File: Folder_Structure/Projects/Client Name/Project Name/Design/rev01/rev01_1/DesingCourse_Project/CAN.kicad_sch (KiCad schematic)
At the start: 0 parts

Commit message: Update 6
SCH and LIB for MOSFET page done, missing passive components
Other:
- company: (none) -> Integro Consulting AB
- title: (none) -> PCB Mastery Project
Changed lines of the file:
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@@
 	(generator_version "9.0")
 	(paper "A4")
+	(title_block
+		(title "PCB Mastery Project")
+		(date "2026-01-27")
+		(rev "001")
+		(company "Integro Consulting AB")
+		(comment 1 "TBD")
+		(comment 2 "TBD")
+		(comment 3 "TBD")
+		(comment 4 "Josue Godinez")
+	)
 )

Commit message: Update 11
SCH finishe, missing the labels and logos and adding all passive components
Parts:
- added C50: 2u2, symbol Device:C
- added C51, C52: 51p, symbol Device:C
- added D15: ESDCAN24-2BLY, ESDCAN24-2BLY:SOT95P237X112-3N, symbol JGB_Library:ESDCAN24-2BLY
- added J1: 874380443, 874380843:MOLEX_874380443, symbol Molex_87438:874380443
- added L1: 744227S, WE-SL2:WE-SL2, symbol WE-SL2:744227S
- added R48, R51: 10R, symbol Device:R
- added R49: 10k, symbol Device:R
- added R50: 120R, symbol Device:R
- added U5: SN65HVD230D, SN65HVD230D:SOIC127P599X175-8N, symbol SN65HVD230D:SN65HVD230D
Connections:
- new net: R49.1, U5.8 (RS)
- new net CAN_N: L1.3, U5.6 (CANL)
- new net CAN_P: L1.4, U5.7 (CANH)
- new net CAN_RX: U5.4 (R)
- new net CAN_TX: U5.1 (D)
- new net CONN_CAN_N: C52.1, D15.2 (A2), J1.3_1 (3), J1.3_2 (3), R50.2, R51.1
- new net CONN_CAN_P: C51.1, D15.1 (A1), J1.2_1 (2), J1.2_2 (2), R48.1, R50.1
- new net GND: C50.2, C51.2, C52.2, D15.3 (C), J1.4_1 (4), J1.4_2 (4), R49.2, U5.2 (GND)
- new net P3V3: C50.1, U5.3 (VCC)
- new net P5V: J1.1_1 (1), J1.1_2 (1)
- new net R_CAN_N: L1.2, R51.2
- new net R_CAN_P: L1.1, R48.2
- no-connect marks 0 -> 1
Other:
- note added: "CAN"
- note added: "CAN_H & CAN_L"
- note added: "Mode selection resistor Slew rate of ~15V/us"
- note added: "Place as close as possible to the IC"
- note added: "ROUTE AS DIFF PAIR"

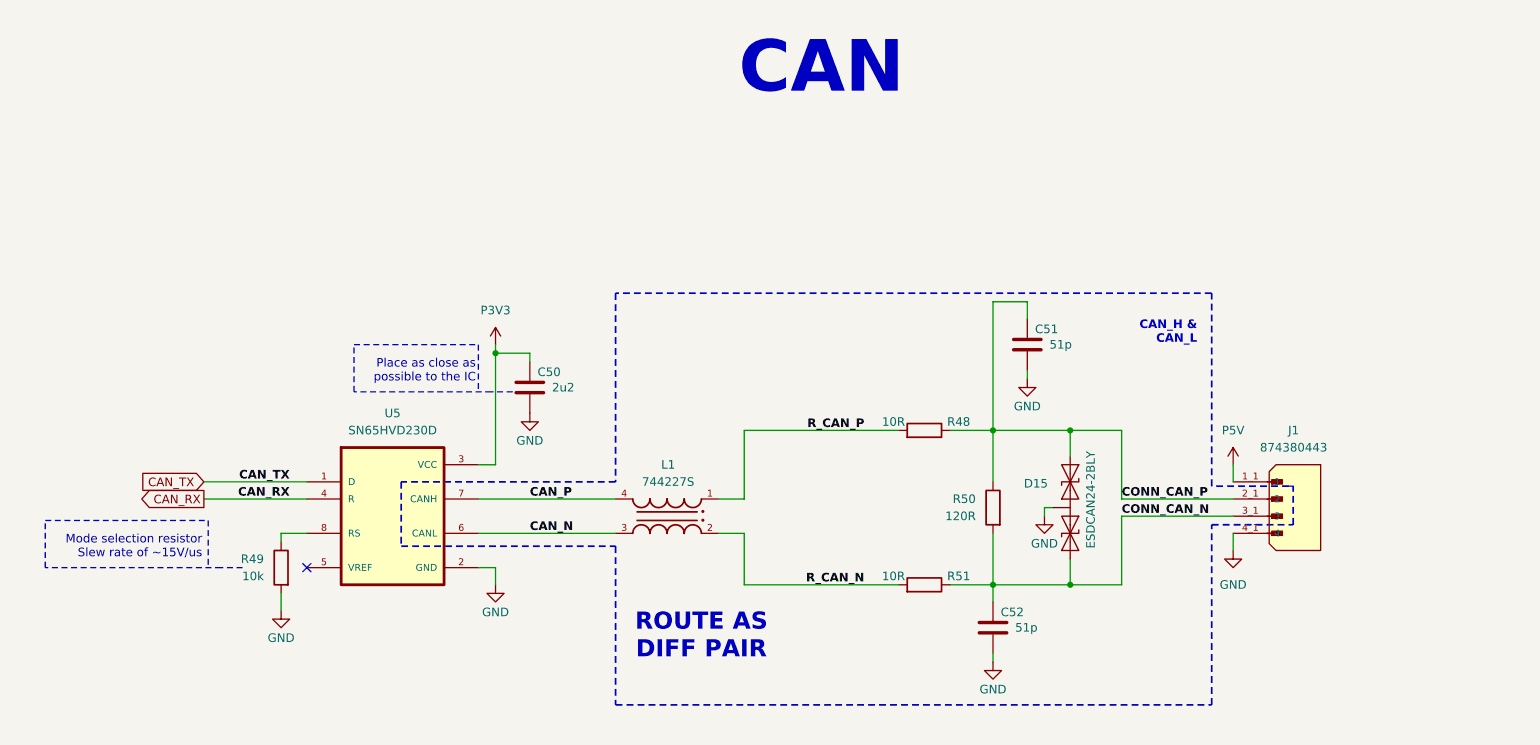
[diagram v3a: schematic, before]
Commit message: Update 12
Until STEP-DOWN page, all components have complete libraries.

Creation and incluison of all logos and labels libraries
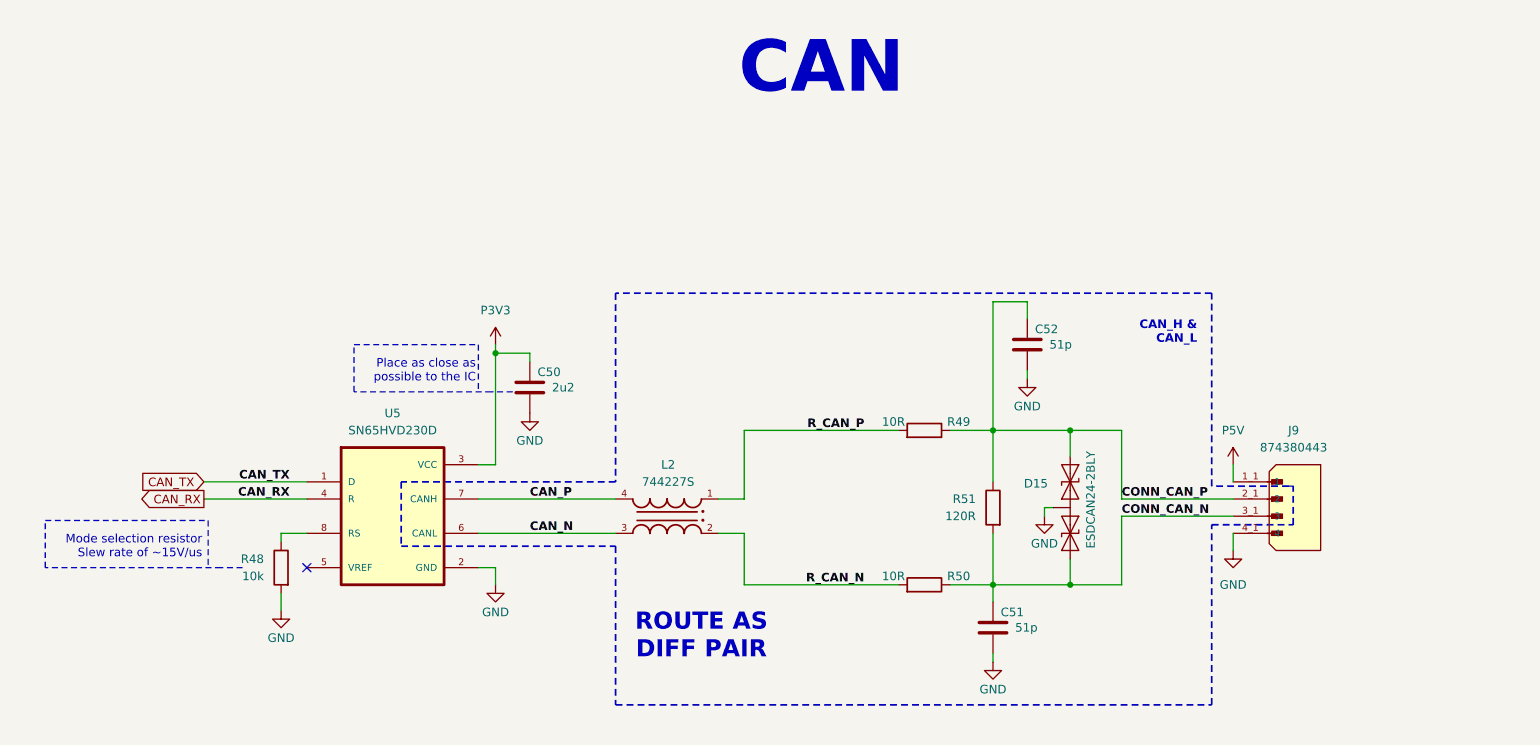
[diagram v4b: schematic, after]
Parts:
- renumbered C52 to C51, C51 to C52, J1 to J9, L1 to L2, R49 to R48, R48 to R49, R51 to R50, R50 to R51

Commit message: Update14
All components with FP, missing the block diagram
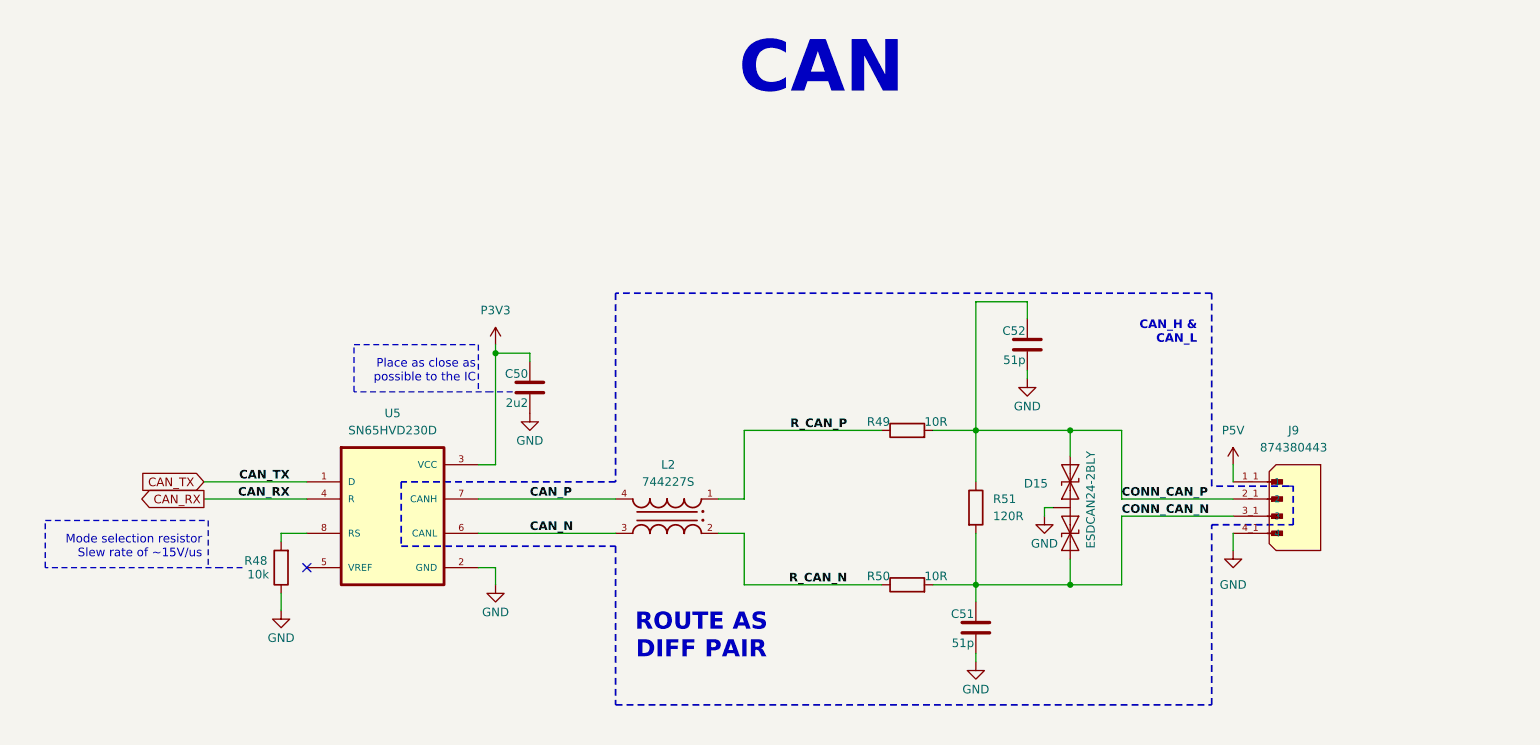
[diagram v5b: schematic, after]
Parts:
- C50: footprint (none) -> Capacitor_SMD:C_0603_1608Metric; Package (none) -> 0603; Temp Coeff (none) -> X5R; Tolerance (none) -> 10%; Voltage Rating (none) -> 6.3V
- C51, C52: footprint (none) -> Capacitor_SMD:C_0603_1608Metric; Package (none) -> 0603; Temp Coeff (none) -> NP0; Tolerance (none) -> 10%; Voltage Rating (none) -> 50V
- R48, R49, R50, R51: footprint (none) -> Resistor_SMD:R_0603_1608Metric; Package (none) -> 0603; Power Rating (none) -> 1/10W; Tolerance (none) -> 1%
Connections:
- net CONN_CAN_N: now also R50.2; no longer R50.1
- net CONN_CAN_P: now also R49.2; no longer R49.1
- net GND: now also R48.1; no longer R48.2
- net R_CAN_N: now also R50.1; no longer R50.2
- net R_CAN_P: now also R49.1; no longer R49.2
- net at U5.8 (RS): now also R48.2; no longer R48.1

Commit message: Update 16
Initial component placement done
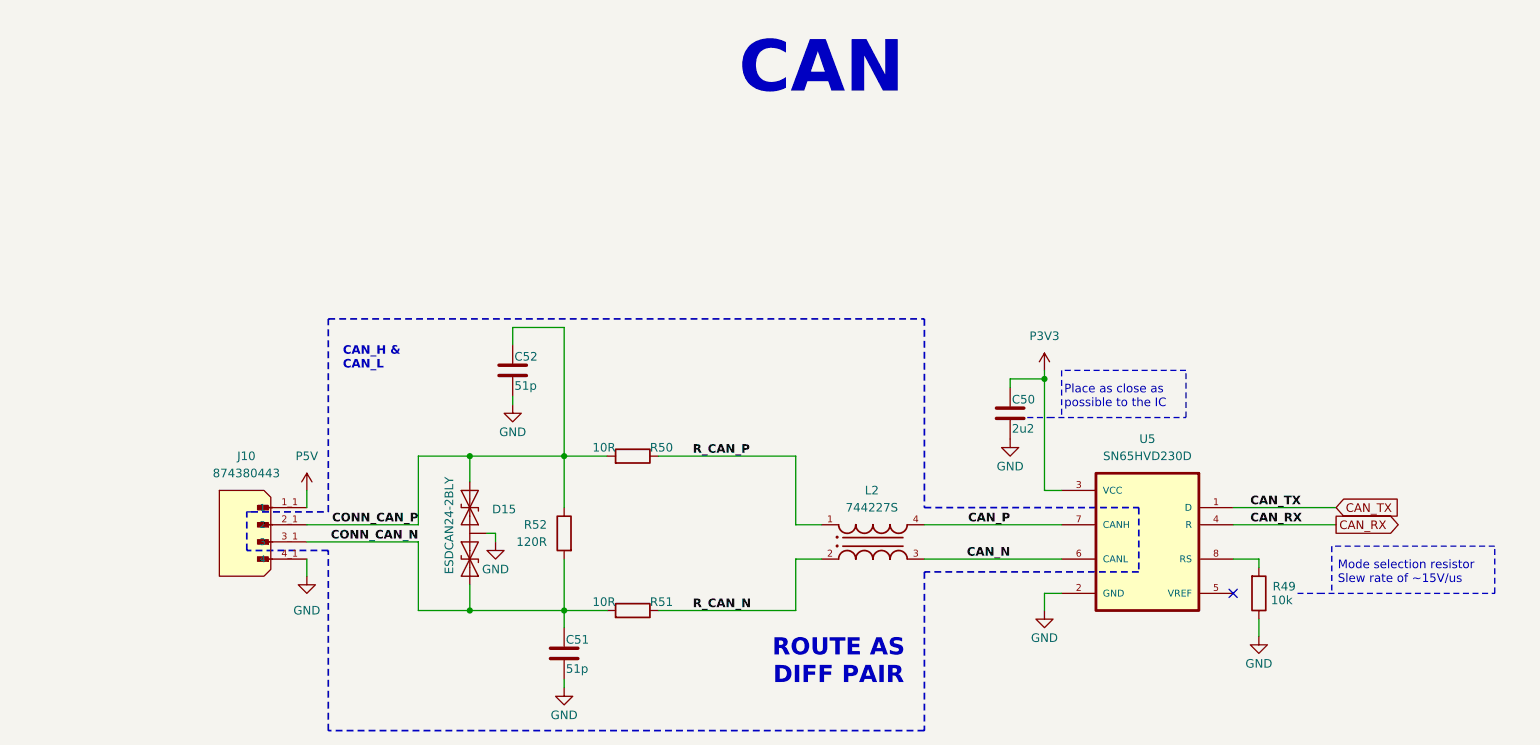
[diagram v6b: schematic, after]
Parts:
- renumbered J9 to J10, R48 to R49, R49 to R50, R50 to R51, R51 to R52
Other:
- moved on the sheet: C50, C51, C52, D15, J10, L2, R49, R50, R51, R52, U5

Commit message: Update17
Design rules and stack defined.

Check againg DR and proceed with layout.
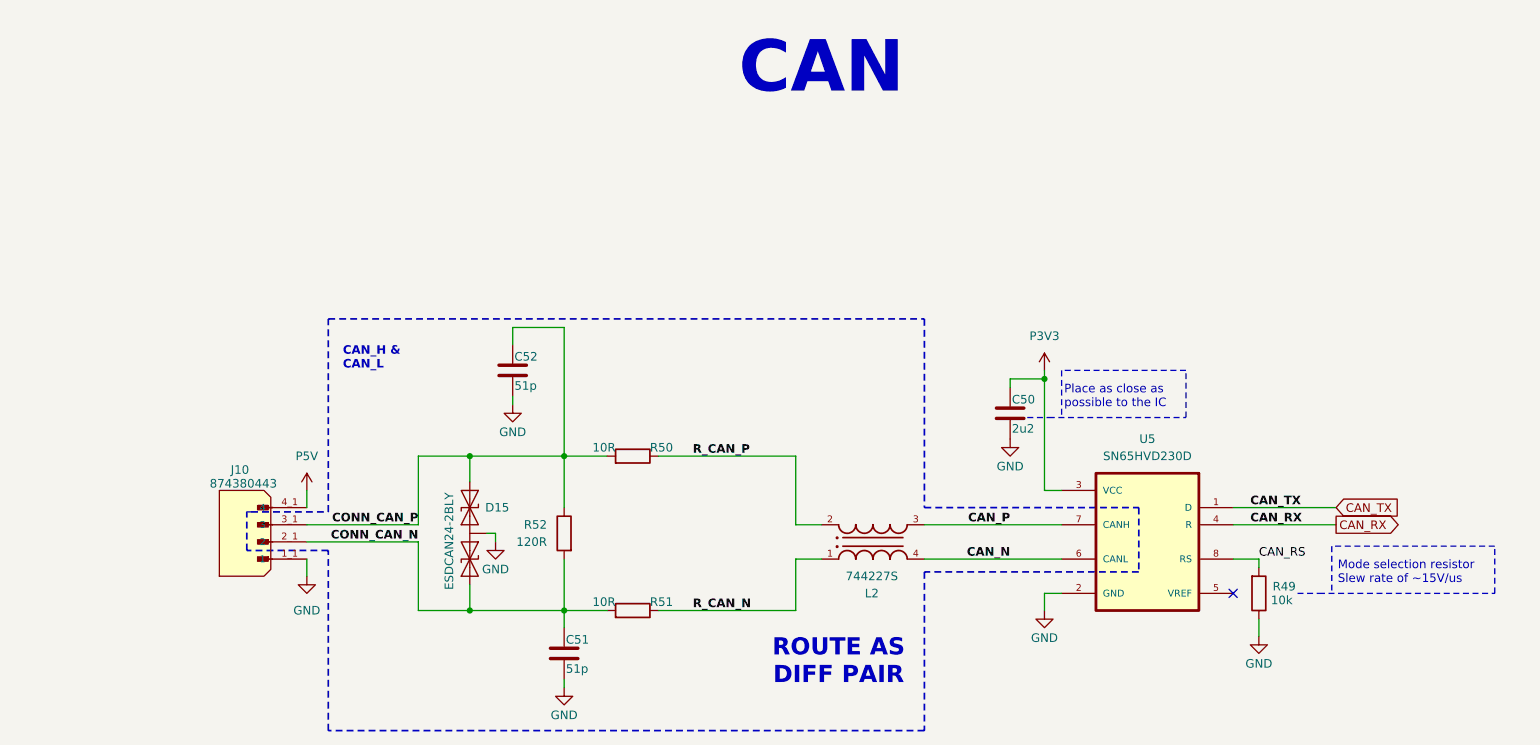
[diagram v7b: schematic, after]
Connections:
- net CAN_N: now also L2.4; no longer L2.3
- net CAN_P: now also L2.3; no longer L2.4
- net CONN_CAN_N: now also D15.1 (A1), J10.2_1 (2), J10.2_2 (2); no longer D15.2 (A2), J10.3_1 (3), J10.3_2 (3)
- net CONN_CAN_P: now also D15.2 (A2), J10.3_1 (3), J10.3_2 (3); no longer D15.1 (A1), J10.2_1 (2), J10.2_2 (2)
- net GND: now also J10.1_1 (1), J10.1_2 (1); no longer J10.4_1 (4), J10.4_2 (4)
- net P5V: now also J10.4_1 (4), J10.4_2 (4); no longer J10.1_1 (1), J10.1_2 (1)
- net R_CAN_N: now also L2.1; no longer L2.2
- net R_CAN_P: now also L2.2; no longer L2.1
- net CAN_RS: now reaches R49.2, U5.8 (RS)
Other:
- moved on the sheet: J10
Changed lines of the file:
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@@
+		)
+	)
+	(label "CAN_RS"
+		(at 224.79 92.71 0)
+		(effects
+			(font
+				(size 1.27 1.27)
+			)
+			(justify left bottom)
 		)
 	)
@@
 	(symbol
 		(lib_id "Molex_87438:874380443")
-		(at 78.74 85.09 0)
-		(mirror y)
+		(at 78.74 92.71 180)
 		(unit 1)
 		(exclude_from_sim no)
@@
 		(on_board yes)
 		(dnp no)
-		(fields_autoplaced yes)
 		(property "Reference" "J10"
-			(at 74.8665 77.47 0)
+			(at 73.914 79.502 0)
 			(effects
 				(font
@@
 		)
 		(property "Value" "874380443"
-			(at 74.8665 80.01 0)
+			(at 74.422 81.534 0)
 			(effects
 				(font
@@
 		)
 		(property "Footprint" "874380843:MOLEX_874380443"
+			(at 78.74 85.09 0)
+			(effects
+				(font
+					(size 1.27 1.27)
+				)
+				(justify bottom)
+				(hide yes)
+			)
+		)
+		(property "Datasheet" ""
 			(at 78.74 92.71 0)
 			(effects
@@
 					(size 1.27 1.27)
 				)
+				(hide yes)
+			)
+		)
+		(property "Description" "Conn Shrouded Header HDR 4 POS 1.5mm Solder RA Side Entry SMD Pico-SPOX™ T/R"
+			(at 78.74 85.09 0)
+			(effects
+				(font
+					(size 1.27 1.27)
+				)
+				(hide yes)
+			)
+		)
+		(property "Manufacturer" "Molex"
+			(at 78.74 85.09 0)
+			(effects
+				(font
+					(size 1.27 1.27)
+				)
 				(justify bottom)
 				(hide yes)
 			)
 		)
-		(property "Datasheet" ""
+		(property "MAXIMUM_PACKAGE_HEIGHT" "4.45 mm"
 			(at 78.74 85.09 0)
 			(effects
@@
 					(size 1.27 1.27)
 				)
-				(hide yes)
-			)
-		)
-		(property "Description" "Conn Shrouded Header HDR 4 POS 1.5mm Solder RA Side Entry SMD Pico-SPOX™ T/R"
+				(justify bottom)
+				(hide yes)
+			)
+		)
+		(property "Package" "SMT"
+			(at 78.74 85.09 0)
+			(effects
+				(font
+					(size 1.27 1.27)
+				)
+				(justify bottom)
+				(hide yes)
+			)
+		)
+		(property "MPN" "874380843"
+			(at 78.74 85.09 0)
+			(effects
+				(font
+					(size 1.27 1.27)
+				)
+				(justify bottom)
+				(hide yes)
+			)
+		)
+		(property "MNP" ""
 			(at 78.74 92.71 0)
 			(effects
@@
 			)
 		)
-		(property "Manufacturer" "Molex"
+		(property "MF" ""
 			(at 78.74 92.71 0)
 			(effects
@@
 					(size 1.27 1.27)
 				)
-				(justify bottom)
-				(hide yes)
-			)
-		)
-		(property "MAXIMUM_PACKAGE_HEIGHT" "4.45 mm"
-			(at 78.74 92.71 0)
-			(effects
-				(font
-					(size 1.27 1.27)
-				)
-				(justify bottom)
-				(hide yes)
-			)
-		)
-		(property "Package" "SMT"
-			(at 78.74 92.71 0)
-			(effects
-				(font
-					(size 1.27 1.27)
-				)
-				(justify bottom)
-				(hide yes)
-			)
-		)
-		(property "MPN" "874380843"
-			(at 78.74 92.71 0)
-			(effects
-				(font
-					(size 1.27 1.27)
-				)
-				(justify bottom)
-				(hide yes)
-			)
-		)
-		(property "MNP" ""
-			(at 78.74 85.09 0)
-			(effects
-				(font
-					(size 1.27 1.27)
-				)
-				(hide yes)
-			)
-		)
-		(property "MF" ""
-			(at 78.74 85.09 0)
-			(effects
-				(font
-					(size 1.27 1.27)
-				)
 				(hide yes)
 			)
@@
 		)
 		(instances
-			(project ""
+			(project "DesingCourse_Project"
 				(path "/e63e39d7-6ac0-4ffd-8aa3-1841a4541b55/4b3fa387-87ed-4757-a85e-cf275a3b7618"
 					(reference "J10")
@@
 		(lib_id "WE-SL2:744227S")
 		(at 167.64 90.17 0)
+		(mirror x)
 		(unit 1)
 		(exclude_from_sim no)
@@
 		(on_board yes)
 		(dnp no)
-		(fields_autoplaced yes)
 		(property "Reference" "L2"
-			(at 167.48 82.55 0)
+			(at 167.48 97.79 0)
 			(effects
 				(font
@@
 		)
 		(property "Value" "744227S"
-			(at 167.48 85.09 0)
+			(at 167.48 95.25 0)
 			(effects
 				(font
@@
 		)
 		(instances
-			(project ""
+			(project "DesingCourse_Project"
 				(path "/e63e39d7-6ac0-4ffd-8aa3-1841a4541b55/4b3fa387-87ed-4757-a85e-cf275a3b7618"
 					(reference "L2")
@@
 		(lib_id "JGB_Library:ESDCAN24-2BLY")
 		(at 107.95 88.9 0)
+		(mirror x)
 		(unit 1)
 		(exclude_from_sim no)
@@
 		(dnp no)
 		(property "Reference" "D15"
-			(at 114.808 85.344 0)
+			(at 113.792 85.09 0)
 			(effects
 				(font
@@
 		)
 		(property "Value" "ESDCAN24-2BLY"
-			(at 104.902 80.518 90)
-			(effects
-				(font
+			(at 104.902 97.282 90)
+			(effects
+				(font
